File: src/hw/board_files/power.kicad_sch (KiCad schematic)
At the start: 33 parts, among them J1 USB_C_Receptacle_USB2.0_14P, J2 Screw_Terminal_01x03, J3 Conn_01x03_Pin, SW1 SW_PWR, U1 MCP73871, U2 TPS63031DSKR

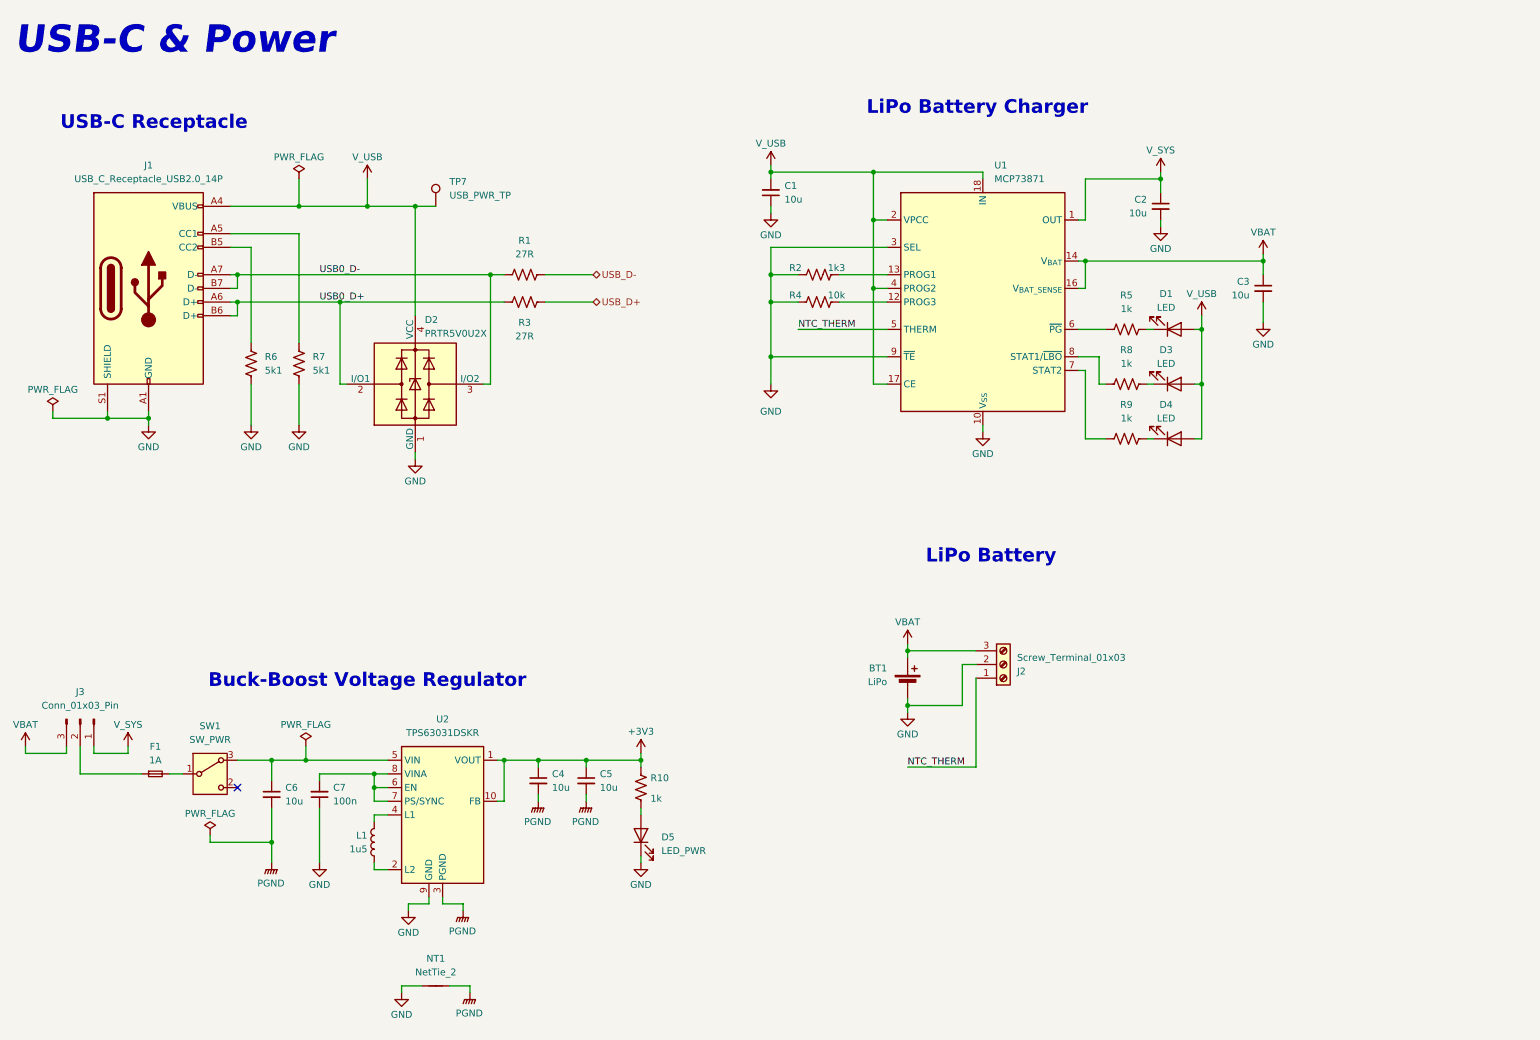
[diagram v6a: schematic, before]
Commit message: Schematic updates
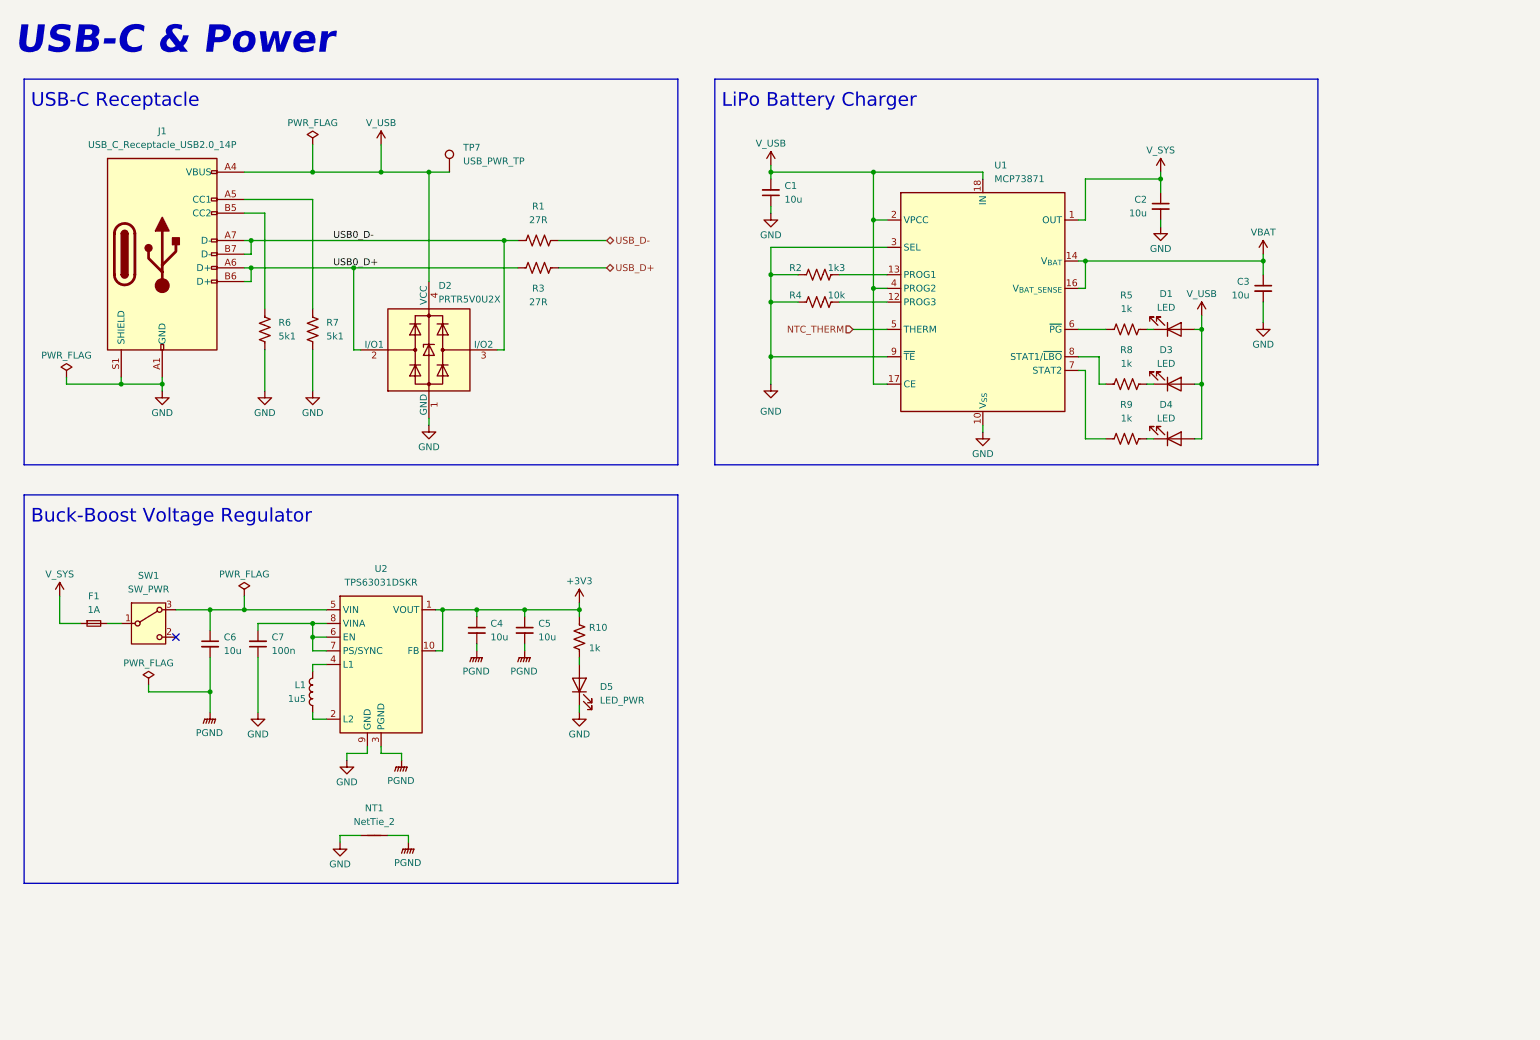
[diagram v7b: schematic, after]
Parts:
- removed BT1: LiPo, Connector_JST:JST_PH_S2B-PH-K_1x02_P2.00mm_Horizontal, symbol Device:Battery_Cell
- removed J2: Screw_Terminal_01x03, TerminalBlock_Phoenix:TerminalBlock_Phoenix_MPT-0,5-3-2.54_1x03_P2.54mm_Horizontal, symbol Connector:Screw_Terminal_01x03
- removed J3: Conn_01x03_Pin, Connector_PinHeader_2.54mm:PinHeader_1x03_P2.54mm_Vertical, symbol Connector:Conn_01x03_Pin
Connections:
- net V_SYS: now also F1.1
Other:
- note removed: "LiPo Battery"
- moved on the sheet: C4, C5, C6, C7, D2, D5, F1, J1, L1, NT1, R1, R10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

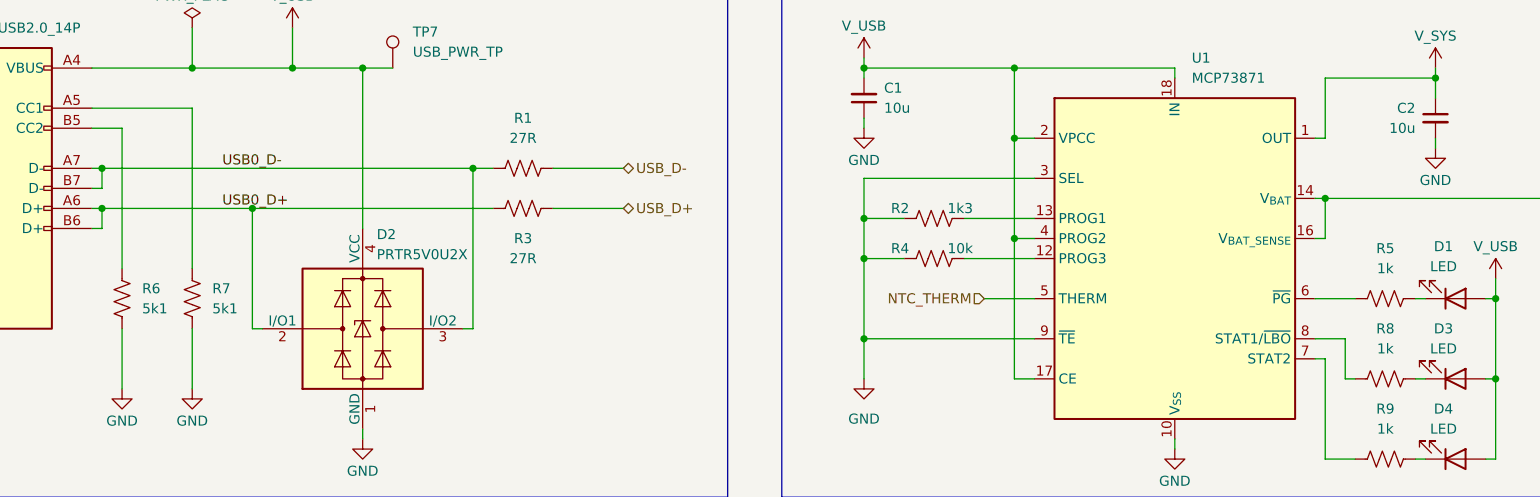
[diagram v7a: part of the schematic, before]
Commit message: Added new OLED footprint. Finished schematic updates, started lyout. Changed 10 mOhm sense resistor PN to TCR of 50 ppm/C
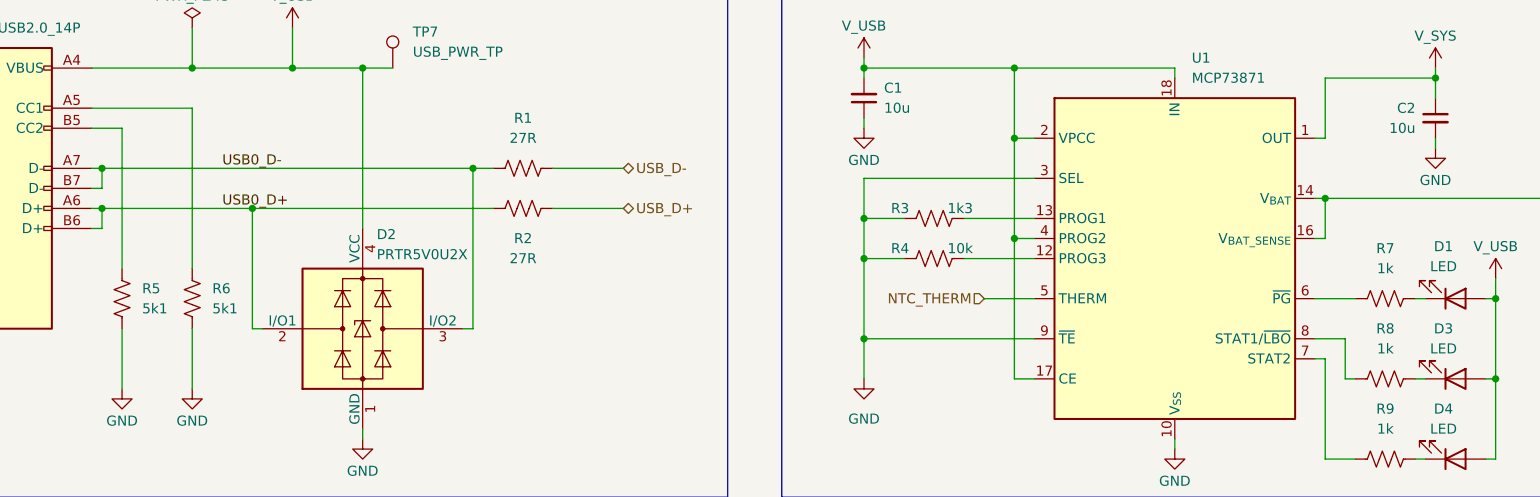
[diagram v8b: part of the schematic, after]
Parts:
- renumbered R3 to R2, R2 to R3, R6 to R5, R7 to R6, R5 to R7
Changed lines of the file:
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@@
 		(on_board yes)
 		(dnp no)
-		(property "Reference" "R2"
+		(property "Reference" "R3"
 			(at 159.512 60.96 90)
 			(effects
@@
 			(project "pocket-caddy"
 				(path "/2c77a8ba-b277-4959-adec-d3fc778c7960/7763c5b3-a08f-479a-9f6f-ea394e6f7159"
-					(reference "R2")
+					(reference "R3")
 					(unit 1)
 				)
@@
 		(on_board yes)
 		(dnp no)
-		(property "Reference" "#PWR018"
+		(property "Reference" "#PWR015"
 			(at 22.86 125.73 0)
 			(effects
@@
 			(project "pocket-caddy"
 				(path "/2c77a8ba-b277-4959-adec-d3fc778c7960/7763c5b3-a08f-479a-9f6f-ea394e6f7159"
-					(reference "#PWR018")
+					(reference "#PWR015")
 					(unit 1)
 				)
@@
 		(on_board yes)
 		(dnp no)
-		(property "Reference" "#PWR014"
+		(property "Reference" "#PWR013"
 			(at 91.44 96.52 0)
 			(effects
@@
 			(project "pocket-caddy"
 				(path "/2c77a8ba-b277-4959-adec-d3fc778c7960/7763c5b3-a08f-479a-9f6f-ea394e6f7159"
-					(reference "#PWR014")
+					(reference "#PWR013")
 					(unit 1)
 				)
@@
 		(on_board yes)
 		(dnp no)
-		(property "Reference" "#PWR013"
+		(property "Reference" "#PWR014"
 			(at 194.31 97.79 0)
 			(effects
@@
 			(project "pocket-caddy"
 				(path "/2c77a8ba-b277-4959-adec-d3fc778c7960/7763c5b3-a08f-479a-9f6f-ea394e6f7159"
-					(reference "#PWR013")
+					(reference "#PWR014")
 					(unit 1)
 				)
@@
 		(on_board yes)
 		(dnp no)
-		(property "Reference" "#PWR01"
+		(property "Reference" "#PWR02"
 			(at 154.94 45.72 0)
 			(effects
@@
 			(project "pocket-caddy"
 				(path "/2c77a8ba-b277-4959-adec-d3fc778c7960/7763c5b3-a08f-479a-9f6f-ea394e6f7159"
-					(reference "#PWR01")
+					(reference "#PWR02")
 					(unit 1)
 				)
@@
 		(dnp no)
 		(fields_autoplaced yes)
-		(property "Reference" "#PWR022"
+		(property "Reference" "#PWR019"
 			(at 50.8 148.59 0)
 			(effects
@@
 			(project ""
 				(path "/2c77a8ba-b277-4959-adec-d3fc778c7960/7763c5b3-a08f-479a-9f6f-ea394e6f7159"
-					(reference "#PWR022")
+					(reference "#PWR019")
 					(unit 1)
 				)
@@
 		(on_board yes)
 		(dnp no)
-		(property "Reference" "#PWR027"
+		(property "Reference" "#PWR024"
 			(at 74.93 173.99 0)
 			(effects
@@
 			(project "pocket-caddy"
 				(path "/2c77a8ba-b277-4959-adec-d3fc778c7960/7763c5b3-a08f-479a-9f6f-ea394e6f7159"
-					(reference "#PWR027")
+					(reference "#PWR024")
 					(unit 1)
 				)
@@
 		(dnp no)
 		(fields_autoplaced yes)
-		(property "Reference" "R7"
+		(property "Reference" "R6"
 			(at 72.39 71.1199 0)
 			(effects
@@
 			(project "pocket-caddy"
 				(path "/2c77a8ba-b277-4959-adec-d3fc778c7960/7763c5b3-a08f-479a-9f6f-ea394e6f7159"
-					(reference "R7")
+					(reference "R6")
 					(unit 1)
 				)
@@
 		(dnp no)
 		(fields_autoplaced yes)
-		(property "Reference" "#PWR028"
+		(property "Reference" "#PWR025"
 			(at 87.63 172.72 0)
 			(effects
@@
 			(project "pocket-caddy"
 				(path "/2c77a8ba-b277-4959-adec-d3fc778c7960/7763c5b3-a08f-479a-9f6f-ea394e6f7159"
-					(reference "#PWR028")
+					(reference "#PWR025")
 					(unit 1)
 				)
@@
 		(on_board yes)
 		(dnp no)
-		(property "Reference" "#PWR019"
+		(property "Reference" "#PWR016"
 			(at 119.38 127 0)
 			(effects
@@
 			(project "pocket-caddy"
 				(path "/2c77a8ba-b277-4959-adec-d3fc778c7960/7763c5b3-a08f-479a-9f6f-ea394e6f7159"
-					(reference "#PWR019")
+					(reference "#PWR016")
 					(unit 1)
 				)
@@
 		(on_board yes)
 		(dnp no)
-		(property "Reference" "#PWR02"
+		(property "Reference" "#PWR03"
 			(at 227.33 46.99 0)
 			(effects
@@
 			(project "pocket-caddy"
 				(path "/2c77a8ba-b277-4959-adec-d3fc778c7960/7763c5b3-a08f-479a-9f6f-ea394e6f7159"
-					(reference "#PWR02")
+					(reference "#PWR03")
 					(unit 1)
 				)
@@
 		(on_board yes)
 		(dnp no)
-		(property "Reference" "#PWR023"
+		(property "Reference" "#PWR020"
 			(at 59.69 149.86 0)
 			(effects
@@
 			(project "pocket-caddy"
 				(path "/2c77a8ba-b277-4959-adec-d3fc778c7960/7763c5b3-a08f-479a-9f6f-ea394e6f7159"
-					(reference "#PWR023")
+					(reference "#PWR020")
 					(unit 1)
 				)
@@
 		(on_board yes)
 		(dnp no)
-		(property "Reference" "#PWR03"
+		(property "Reference" "#PWR01"
 			(at 82.55 41.91 0)
 			(effects
@@
 			(project "pocket-caddy"
 				(path "/2c77a8ba-b277-4959-adec-d3fc778c7960/7763c5b3-a08f-479a-9f6f-ea394e6f7159"
-					(reference "#PWR03")
+					(reference "#PWR01")
 					(unit 1)
 				)
@@
 		(on_board yes)
 		(dnp no)
-		(property "Reference" "#PWR025"
+		(property "Reference" "#PWR022"
 			(at 76.2 158.75 0)
 			(effects
@@
 			(project "pocket-caddy"
 				(path "/2c77a8ba-b277-4959-adec-d3fc778c7960/7763c5b3-a08f-479a-9f6f-ea394e6f7159"
-					(reference "#PWR025")
+					(reference "#PWR022")
 					(unit 1)
 				)
@@
 		(dnp no)
 		(fields_autoplaced yes)
-		(property "Reference" "R5"
+		(property "Reference" "R7"
 			(at 220.98 66.04 90)
 			(effects
@@
 			(project "pocket-caddy"
 				(path "/2c77a8ba-b277-4959-adec-d3fc778c7960/7763c5b3-a08f-479a-9f6f-ea394e6f7159"
-					(reference "R5")
+					(reference "R7")
 					(unit 1)
 				)
@@
 		(dnp no)
 		(fields_autoplaced yes)
-		(property "Reference" "R3"
+		(property "Reference" "R2"
 			(at 111.76 64.77 90)
 			(effects
@@
 			(project "pocket-caddy"
 				(path "/2c77a8ba-b277-4959-adec-d3fc778c7960/7763c5b3-a08f-479a-9f6f-ea394e6f7159"
-					(reference "R3")
+					(reference "R2")
 					(unit 1)
 				)
@@
 		(on_board yes)
 		(dnp no)
-		(property "Reference" "#PWR024"
+		(property "Reference" "#PWR021"
 			(at 119.38 149.86 0)
 			(effects
@@
 			(project "pocket-caddy"
 				(path "/2c77a8ba-b277-4959-adec-d3fc778c7960/7763c5b3-a08f-479a-9f6f-ea394e6f7159"
-					(reference "#PWR024")
+					(reference "#PWR021")
 					(unit 1)
 				)
@@
 		(dnp no)
 		(fields_autoplaced yes)
-		(property "Reference" "#PWR020"
+		(property "Reference" "#PWR017"
 			(at 100.33 137.16 0)
 			(effects
@@
 			(project "pocket-caddy"
 				(path "/2c77a8ba-b277-4959-adec-d3fc778c7960/7763c5b3-a08f-479a-9f6f-ea394e6f7159"
-					(reference "#PWR020")
+					(reference "#PWR017")
 					(unit 1)
 				)
@@
 		(dnp no)
 		(fields_autoplaced yes)
-		(property "Reference" "#PWR021"
+		(property "Reference" "#PWR018"
 			(at 109.22 137.16 0)
 			(effects
@@
 			(project "pocket-caddy"
 				(path "/2c77a8ba-b277-4959-adec-d3fc778c7960/7763c5b3-a08f-479a-9f6f-ea394e6f7159"
-					(reference "#PWR021")
+					(reference "#PWR018")
 					(unit 1)
 				)
@@
 		(dnp no)
 		(fields_autoplaced yes)
-		(property "Reference" "#PWR026"
+		(property "Reference" "#PWR023"
 			(at 86.36 157.48 0)
 			(effects
@@
 			(project "pocket-caddy"
 				(path "/2c77a8ba-b277-4959-adec-d3fc778c7960/7763c5b3-a08f-479a-9f6f-ea394e6f7159"
-					(reference "#PWR026")
+					(reference "#PWR023")
 					(unit 1)
 				)
@@
 		(dnp no)
 		(fields_autoplaced yes)
-		(property "Reference" "R6"
+		(property "Reference" "R5"
 			(at 63.5 71.1199 0)
 			(effects
@@
 			(project "pocket-caddy"
 				(path "/2c77a8ba-b277-4959-adec-d3fc778c7960/7763c5b3-a08f-479a-9f6f-ea394e6f7159"
-					(reference "R6")
+					(reference "R5")
 					(unit 1)
 				)
